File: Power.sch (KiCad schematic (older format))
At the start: 7 parts, among them U1 LM3940IMP-3.3

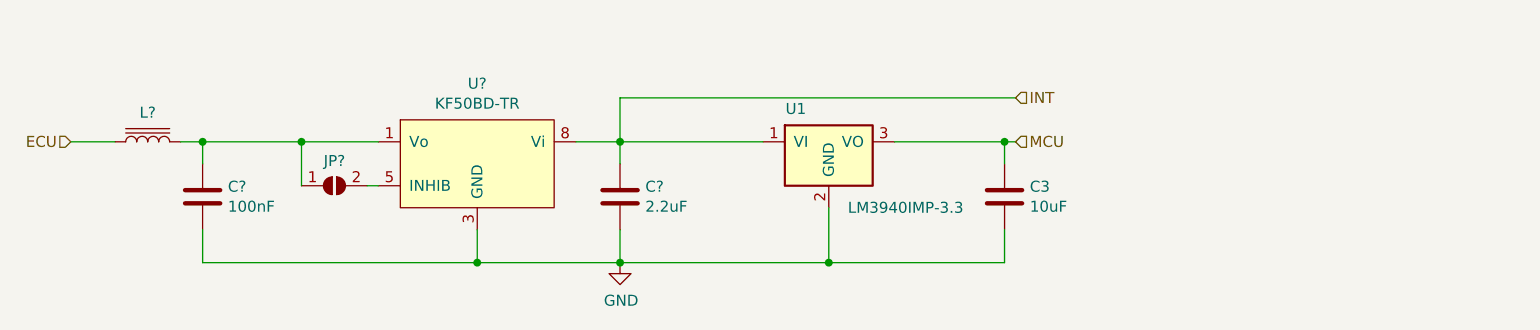
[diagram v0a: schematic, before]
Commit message: corrected CAN schematic
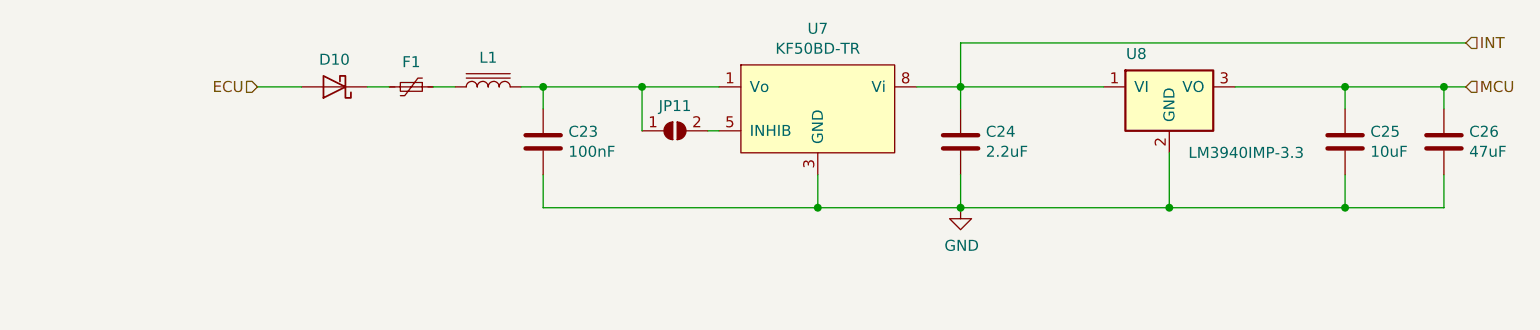
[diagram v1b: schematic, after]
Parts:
- added C26: 47uF, Capacitor_SMD:C_0805_2012Metric, symbol Device:C
- added D10: MBR0530T1G, Diode_SMD:D_SOD-123, symbol Device:D_Schottky
- added F1: 1206L025YR, Fuse:Fuse_1206_3216Metric, symbol Device:Polyfuse_Small
- C23: renamed from C?; footprint Capacitor_SMD:C_0805_2012Metric -> Capacitor_SMD:C_0603_1608Metric; Description (none) -> 100nF ±10% 100V X7R 0603 Multilayer Ceramic Capacitors; Manufacturer (none) -> Samsung Electro-Mechanics; Mount (none) -> MOUNT; MountType (none) -> SMD; PartNumber (none) -> CL10B104KC8NNNC
- C24: renamed from C?; Description (none) -> 2.2uF -20%,+80% 10V Y5V 0805 Multilayer Ceramic Capacitors; Manufacturer (none) -> Samsung Electro-Mechanics; Mount (none) -> MOUNT; MountType (none) -> SMD; PartNumber (none) -> CL21F225ZPFNNNE
- C25: renamed from C3; Description MULTILAYER CERAMIC CAPACITORS MLCC - SMD/SMT 10UF 25V 0805 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 -> 10uF ±10% 10V X5R 0805 Multilayer Ceramic Capacitors MLCC; PartNumber CL21A106KAYNNNE -> CL21A106KPFNNNE
- JP11: renamed from JP?; footprint (none) -> Jumper:SolderJumper-2_P1.3mm_Open_RoundedPad1.0x1.5mm; Description (none) -> NOT A COMPONENT; Manufacturer (none) -> NOT A COMPONENT; Mount (none) -> DO NOT MOUNT; MountType (none) -> SMD; PartNumber (none) -> NOT A COMPONENT
- L1: renamed from L?; Manufacturer (none) -> -; Mount (none) -> MOUNT; MountType (none) -> SMD
- U7: renamed from U?; Description (none) -> LDO 20V fixed output 5V 700mV @ 500mA SOIC-8_150mil; Manufacturer (none) -> ST Microelectronics; Mount (none) -> MOUNT; MountType (none) -> SMD; PartNumber (none) -> KF50BD-TR
- renumbered U1 to U8
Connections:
- net ECU: now also D10.2 (A); no longer L1.1
- net GND: now also C26.2
- net MCU: now also C26.1
- new net: F1.1, L1.1
- new net: D10.1 (K), F1.2
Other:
- moved on the sheet: C23, C24, C25, JP11, L1, U7, U8

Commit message: Start routing
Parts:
- added D10: 5KP15CA, Diode_THT:D_5KP_P10.16mm_Horizontal, symbol Device:D_TVS
- L1: footprint (none) -> Inductor_SMD:L_1206_3216Metric
- renumbered D10 to D11
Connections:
- net ECU: now also F1.2; no longer D11.2 (A)
- net GND: now also D10.2 (A2)
- net at C23.1, JP11.1 (A), U7.1 (Vo): now also D11.1 (K); no longer L1.2
- net at F1.1, L1.1: now also D10.1 (A1)
- new net: D11.2 (A), L1.2
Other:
- moved on the sheet: D11, F1, L1
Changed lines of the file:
@@
 Comment4 ""
 $EndDescr
-Text HLabel 1800 2700 0    50   Input ~ 0
+Text HLabel 1650 2700 0    50   Input ~ 0
 ECU
 $Comp
@@
 L Device:L_Core_Iron L1
 U 1 1 600A9E46
-P 2850 2700
-F 0 "L1" V 2983 2700 50  0000 C CNN
-F 1 "L_Core_Iron" V 2984 2700 50  0001 C CNN
-F 2 "" H 2850 2700 50  0001 C CNN
-F 3 "~" H 2850 2700 50  0001 C CNN
-F 4 "MOUNT" H 2850 2700 50  0001 C CNN "Mount"
-F 5 "SMD" H 2850 2700 50  0001 C CNN "MountType"
-F 6 "-" H 2850 2700 50  0001 C CNN "Manufacturer"
-	1    2850 2700
+P 2450 2700
+F 0 "L1" V 2583 2700 50  0000 C CNN
+F 1 "L_Core_Iron" V 2584 2700 50  0001 C CNN
+F 2 "Inductor_SMD:L_1206_3216Metric" H 2450 2700 50  0001 C CNN
+F 3 "~" H 2450 2700 50  0001 C CNN
+F 4 "MOUNT" H 2450 2700 50  0001 C CNN "Mount"
+F 5 "SMD" H 2450 2700 50  0001 C CNN "MountType"
+F 6 "-" H 2450 2700 50  0001 C CNN "Manufacturer"
+	1    2450 2700
 	0    -1   -1   0
 $EndComp
@@
 	3100 2700 3100 2800
 Connection ~ 3100 2700
-Wire Wire Line
-	1800 2700 2000 2700
 Wire Wire Line
 	4800 2700 5000 2700
@@
 	7200 2700 7300 2700
 $Comp
-L Device:D_Schottky D10
+L Device:D_Schottky D11
 U 1 1 600DD919
-P 2150 2700
-F 0 "D10" H 2150 2576 50  0000 C CNN
-F 1 "MBR0530T1G" H 2150 2575 50  0001 C CNN
-F 2 "Diode_SMD:D_SOD-123" H 2150 2700 50  0001 C CNN
-F 3 "https://datasheet.lcsc.com/szlcsc/ON-Semicon-ON-MBR0530T1G_C82046.pdf" H 2150 2700 50  0001 C CNN
-F 4 "30V 500mA 430mV @ 500mA SOD-123 Schottky Barrier Diodes" H 2150 2700 50  0001 C CNN "Description"
-F 5 "ON Semiconductor" H 2150 2700 50  0001 C CNN "Manufacturer"
-F 6 "MOUNT" H 2150 2700 50  0001 C CNN "Mount"
-F 7 "SMD" H 2150 2700 50  0001 C CNN "MountType"
-F 8 "MBR0530T1G" H 2150 2700 50  0001 C CNN "PartNumber"
-	1    2150 2700
+P 2850 2700
+F 0 "D11" H 2850 2450 50  0000 C CNN
+F 1 "MBR0530T1G" H 2800 2550 50  0000 C CNN
+F 2 "Diode_SMD:D_SOD-123" H 2850 2700 50  0001 C CNN
+F 3 "https://datasheet.lcsc.com/szlcsc/ON-Semicon-ON-MBR0530T1G_C82046.pdf" H 2850 2700 50  0001 C CNN
+F 4 "30V 500mA 430mV @ 500mA SOD-123 Schottky Barrier Diodes" H 2850 2700 50  0001 C CNN "Description"
+F 5 "ON Semiconductor" H 2850 2700 50  0001 C CNN "Manufacturer"
+F 6 "MOUNT" H 2850 2700 50  0001 C CNN "Mount"
+F 7 "SMD" H 2850 2700 50  0001 C CNN "MountType"
+F 8 "MBR0530T1G" H 2850 2700 50  0001 C CNN "PartNumber"
+	1    2850 2700
 	-1   0    0    1
 $EndComp
@@
 L Device:Polyfuse_Small F1
 U 1 1 600DEBDF
-P 2500 2700
-F 0 "F1" V 2387 2700 50  0000 C CNN
-F 1 "1206L025YR" V 2386 2700 50  0001 C CNN
-F 2 "Fuse:Fuse_1206_3216Metric" H 2550 2500 50  0001 L CNN
-F 3 "https://datasheet.lcsc.com/szlcsc/Littelfuse-1206L025YR_C99561.pdf" H 2500 2700 50  0001 C CNN
-F 4 "Polymeric 16V 500mA 100ms 750mΩ 1206 PTC Resettable Fuses RoHS" H 2500 2700 50  0001 C CNN "Description"
-F 5 "Littelfuse" H 2500 2700 50  0001 C CNN "Manufacturer"
-F 6 "MOUNT" H 2500 2700 50  0001 C CNN "Mount"
-F 7 "SMD" H 2500 2700 50  0001 C CNN "MountType"
-F 8 "1206L025YR" H 2500 2700 50  0001 C CNN "PartNumber"
-	1    2500 2700
+P 1900 2700
+F 0 "F1" V 1787 2700 50  0000 C CNN
+F 1 "1206L025YR" V 1786 2700 50  0001 C CNN
+F 2 "Fuse:Fuse_1206_3216Metric" H 1950 2500 50  0001 L CNN
+F 3 "https://datasheet.lcsc.com/szlcsc/Littelfuse-1206L025YR_C99561.pdf" H 1900 2700 50  0001 C CNN
+F 4 "Polymeric 16V 500mA 100ms 750mΩ 1206 PTC Resettable Fuses RoHS" H 1900 2700 50  0001 C CNN "Description"
+F 5 "Littelfuse" H 1900 2700 50  0001 C CNN "Manufacturer"
+F 6 "MOUNT" H 1900 2700 50  0001 C CNN "Mount"
+F 7 "SMD" H 1900 2700 50  0001 C CNN "MountType"
+F 8 "1206L025YR" H 1900 2700 50  0001 C CNN "PartNumber"
+	1    1900 2700
 	0    1    1    0
 $EndComp
 Wire Wire Line
-	2300 2700 2400 2700
-Wire Wire Line
-	2600 2700 2700 2700
+	2000 2700 2200 2700
+$Comp
+L Device:D_TVS D10
+U 1 1 600F6140
+P 2200 2950
+F 0 "D10" V 2154 3029 50  0000 L CNN
+F 1 "5KP15CA" V 2245 3029 50  0000 L CNN
+F 2 "Diode_THT:D_5KP_P10.16mm_Horizontal" H 2200 2950 50  0001 C CNN
+F 3 "https://m.littelfuse.com/~/media/electronics/datasheets/tvs_diodes/littelfuse_tvs_diode_5kp_datasheet.pdf.pdf" H 2200 2950 50  0001 C CNN
+	1    2200 2950
+	0    1    1    0
+$EndComp
+Wire Wire Line
+	2700 2700 2600 2700
+Wire Wire Line
+	2200 2700 2200 2800
+Wire Wire Line
+	2200 3100 2200 3250
+Connection ~ 3100 3250
+Connection ~ 2200 2700
+Wire Wire Line
+	2200 2700 2300 2700
+Wire Wire Line
+	1650 2700 1800 2700
+Wire Wire Line
+	2200 3250 3100 3250
 $EndSCHEMATC

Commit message: CAN part routing
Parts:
- renumbered C23 to C25, C24 to C26, C25 to C27, C26 to C28
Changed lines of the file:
@@
 $EndComp
 $Comp
-L Device:C C25
+L Device:C C27
 U 1 1 5FDFBDAA
 P 6750 2950
-F 0 "C25" H 6865 2996 50  0000 L CNN
+F 0 "C27" H 6865 2996 50  0000 L CNN
 F 1 "10uF" H 6865 2905 50  0000 L CNN
 F 2 "Capacitor_SMD:C_0805_2012Metric" H 6788 2800 50  0001 C CNN
@@
 INT
 $Comp
-L Device:C C23
+L Device:C C25
 U 1 1 600A96CB
 P 3100 2950
-F 0 "C23" H 3215 2996 50  0000 L CNN
+F 0 "C25" H 3215 2996 50  0000 L CNN
 F 1 "100nF" H 3215 2905 50  0000 L CNN
 F 2 "Capacitor_SMD:C_0603_1608Metric" H 3138 2800 50  0001 C CNN
@@
 $EndComp
 $Comp
-L Device:C C24
+L Device:C C26
 U 1 1 600A99AE
 P 5000 2950
-F 0 "C24" H 5115 2996 50  0000 L CNN
+F 0 "C26" H 5115 2996 50  0000 L CNN
 F 1 "2.2uF" H 5115 2905 50  0000 L CNN
 F 2 "Capacitor_SMD:C_0805_2012Metric" H 5038 2800 50  0001 C CNN
@@
 	3550 2700 3900 2700
 $Comp
-L power:GND #PWR041
+L power:GND #PWR043
 U 1 1 600BCBD7
 P 5000 3250
-F 0 "#PWR041" H 5000 3000 50  0001 C CNN
+F 0 "#PWR043" H 5000 3000 50  0001 C CNN
 F 1 "GND" H 5005 3077 50  0000 C CNN
 F 2 "" H 5000 3250 50  0001 C CNN
@@
 $EndComp
 $Comp
-L Device:C C26
+L Device:C C28
 U 1 1 600C642E
 P 7200 2950
-F 0 "C26" H 7315 2996 50  0000 L CNN
+F 0 "C28" H 7315 2996 50  0000 L CNN
 F 1 "47uF" H 7315 2905 50  0000 L CNN
 F 2 "Capacitor_SMD:C_0805_2012Metric" H 7238 2800 50  0001 C CNN
